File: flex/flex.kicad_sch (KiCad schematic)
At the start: 18 parts, among them J1 Conn_01x06_Female, J2 Conn_01x03_Female, SW19 SW_Push, SW5 SW_Push, SW9 SW_Push

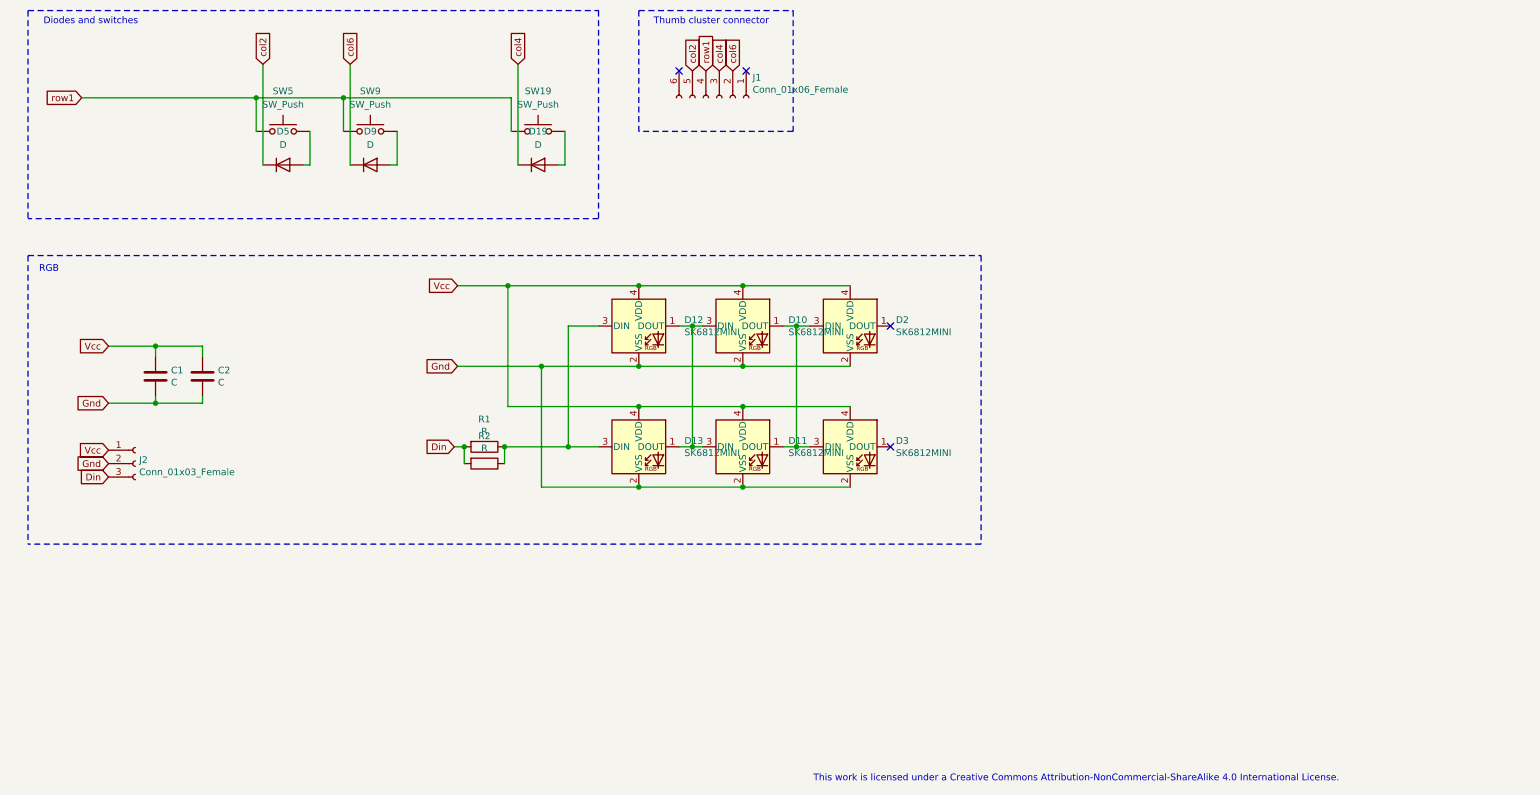
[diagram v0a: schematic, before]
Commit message: sch: update symbols from library and fix erc
Signed-off-by: Anant Thazhemadam <anant.thazhemadam@gmail.com>
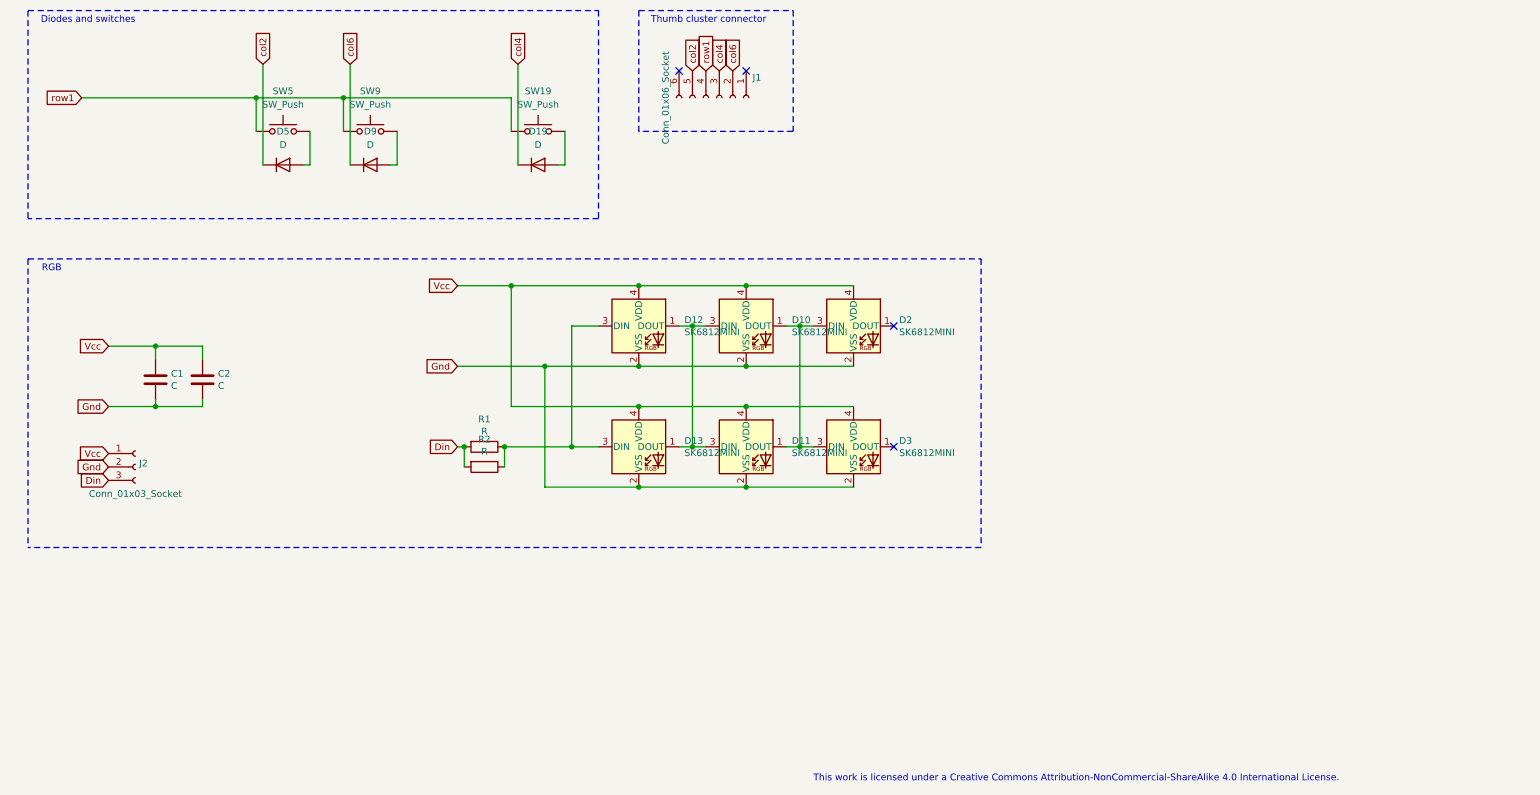
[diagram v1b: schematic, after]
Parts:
- D10, D12, D2: footprint libs2:YS-SK6812MINI-E_REVERSE -> LED_SMD:LED_SK6812MINI_PLCC4_3.5x3.5mm_P1.75mm
- D11, D13, D3: footprint libs2:YS-SK6812MINI-E_REVERSE_NO_EDGECUT -> LED_SMD:LED_SK6812MINI_PLCC4_3.5x3.5mm_P1.75mm
- J1: value Conn_01x06_Female -> Conn_01x06_Socket; footprint Connector_PinHeader_2.54mm:PinHeader_1x06_P2.54mm_Vertical -> (none); symbol Connector:Conn_01x06_Female -> Connector:Conn_01x06_Socket
- J2: value Conn_01x03_Female -> Conn_01x03_Socket; footprint Connector_PinHeader_2.54mm:PinHeader_1x03_P2.54mm_Vertical -> (none); symbol Connector:Conn_01x03_Female -> Connector:Conn_01x03_Socket
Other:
- moved on the sheet: C1, C2, D10, D11, D2, D3, J2, R2

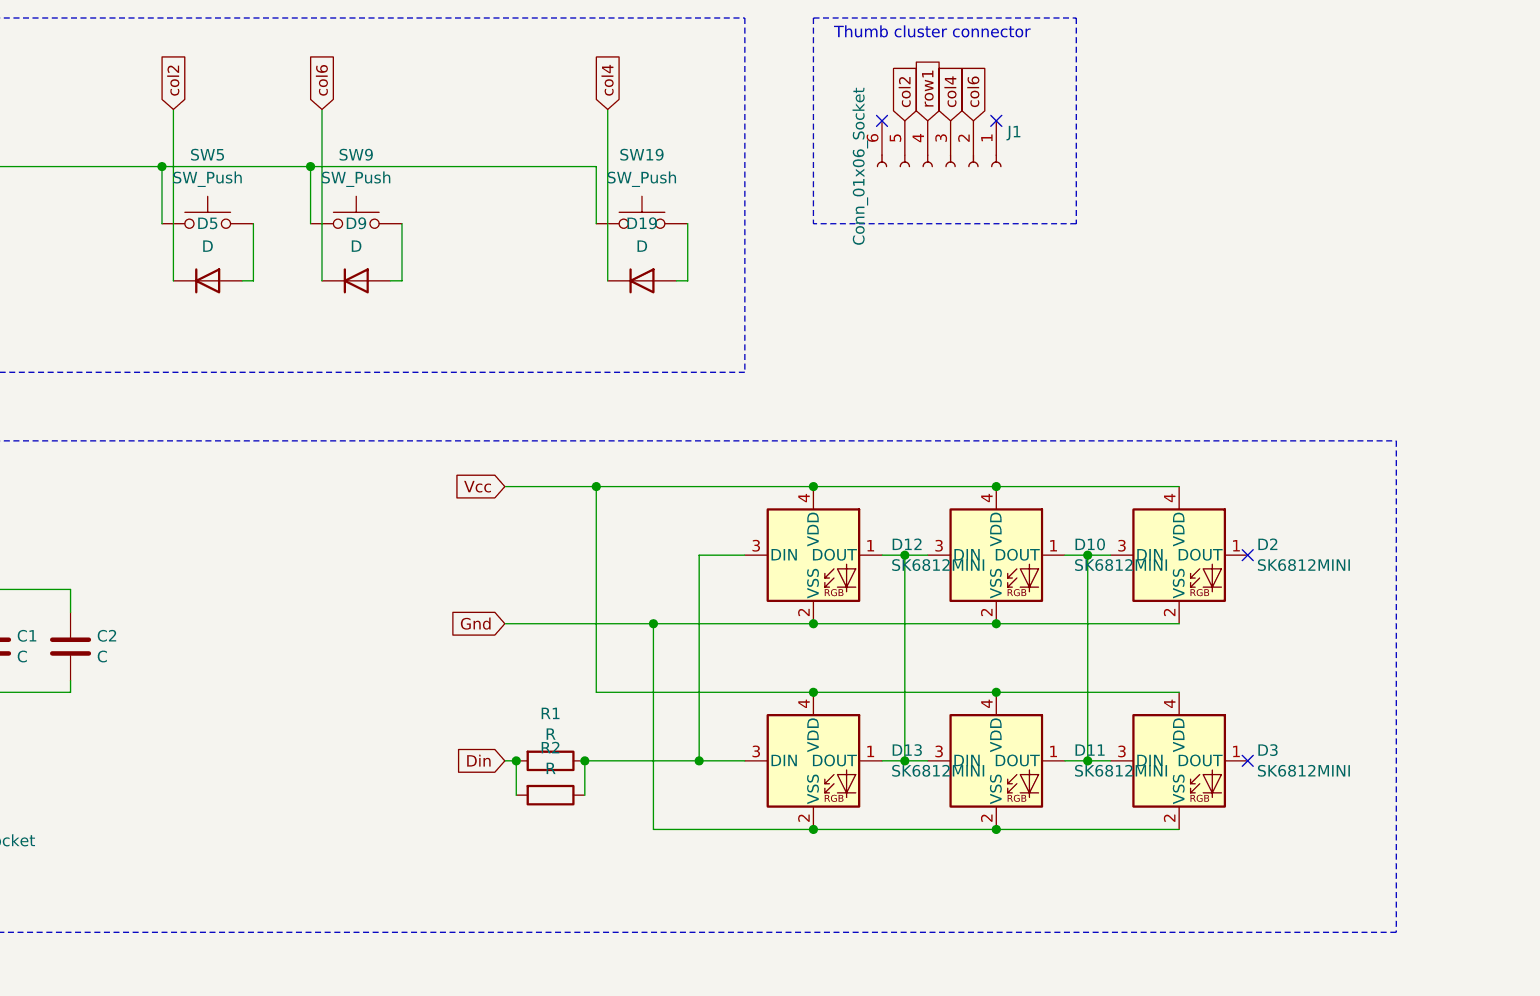
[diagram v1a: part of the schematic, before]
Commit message: remove breakaway thumb
Signed-off-by: Anant Thazhemadam <anant.thazhemadam@gmail.com>
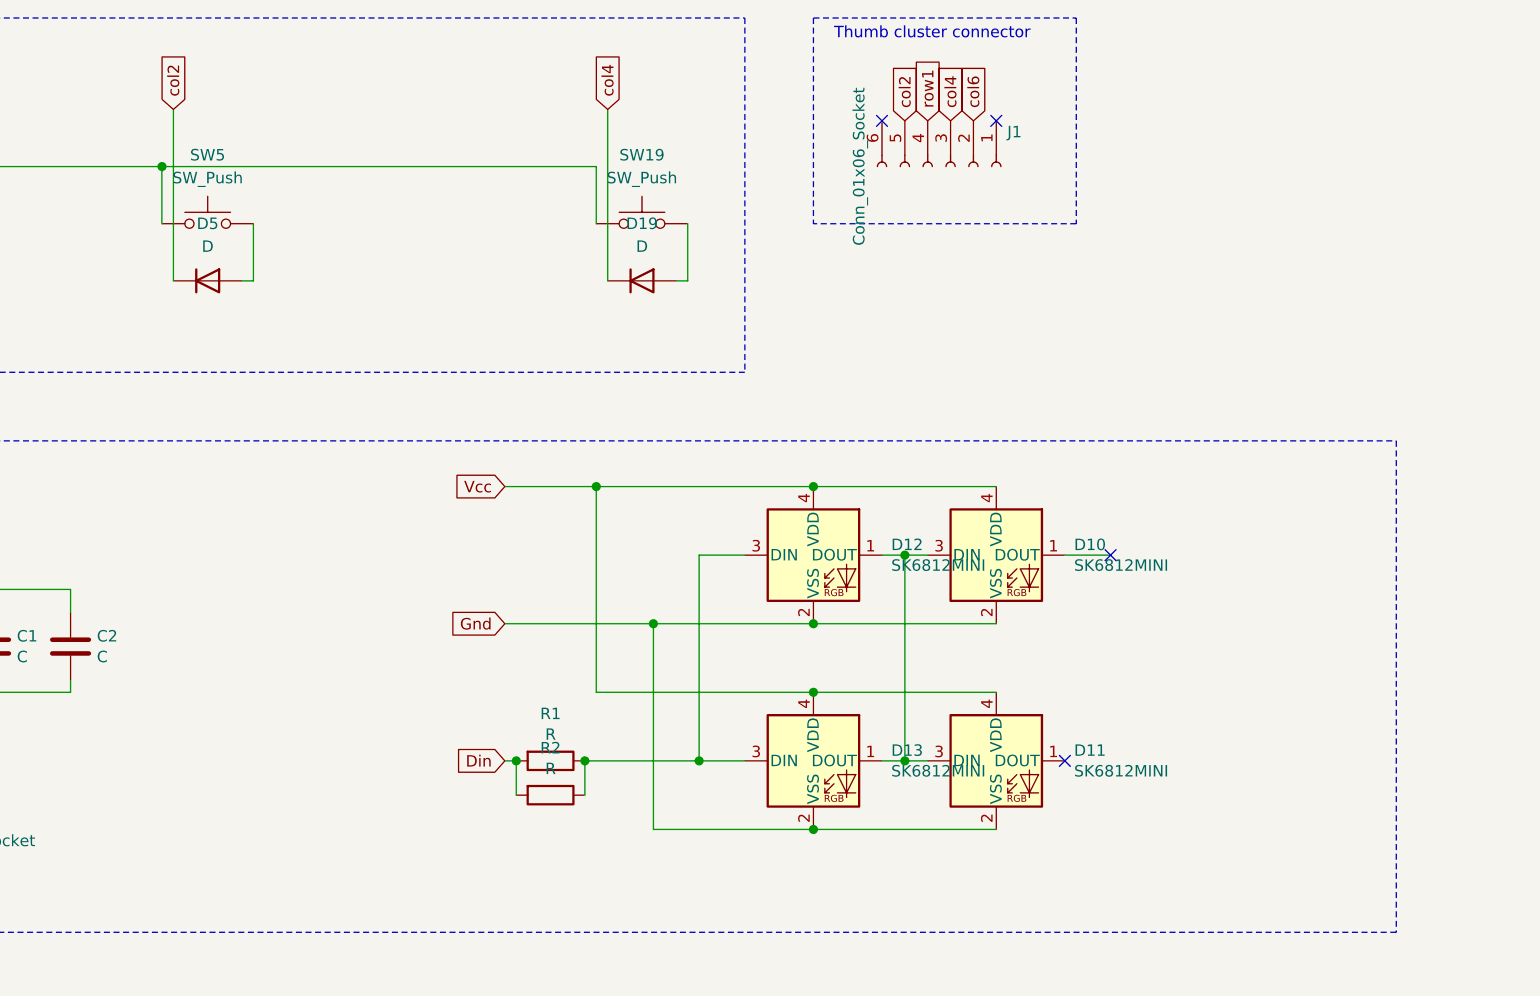
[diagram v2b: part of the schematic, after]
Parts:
- removed D2, D3: SK6812MINI, LED_SMD:LED_SK6812MINI_PLCC4_3.5x3.5mm_P1.75mm, symbol LED:SK6812MINI
- removed D9: D, custom:Diode_TH_SOD123, symbol Device:D
- removed SW9: SW_Push, custom:SW_MX_reversible, symbol Switch:SW_Push
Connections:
- net at D10.1 (DOUT): no longer D11.1 (DOUT)
